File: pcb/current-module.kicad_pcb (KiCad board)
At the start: 4 copper layers, 50 x 50 mm, 128 parts, among them J2 SWD Header, SW1 SKRPABE010, U1 STM32C051G8Ux, U2 A1324LLHLT-T, U3 A1324LLHLT-T, U4 TLV9064, Y1 ECS-480-10-37B2-RWN-TR

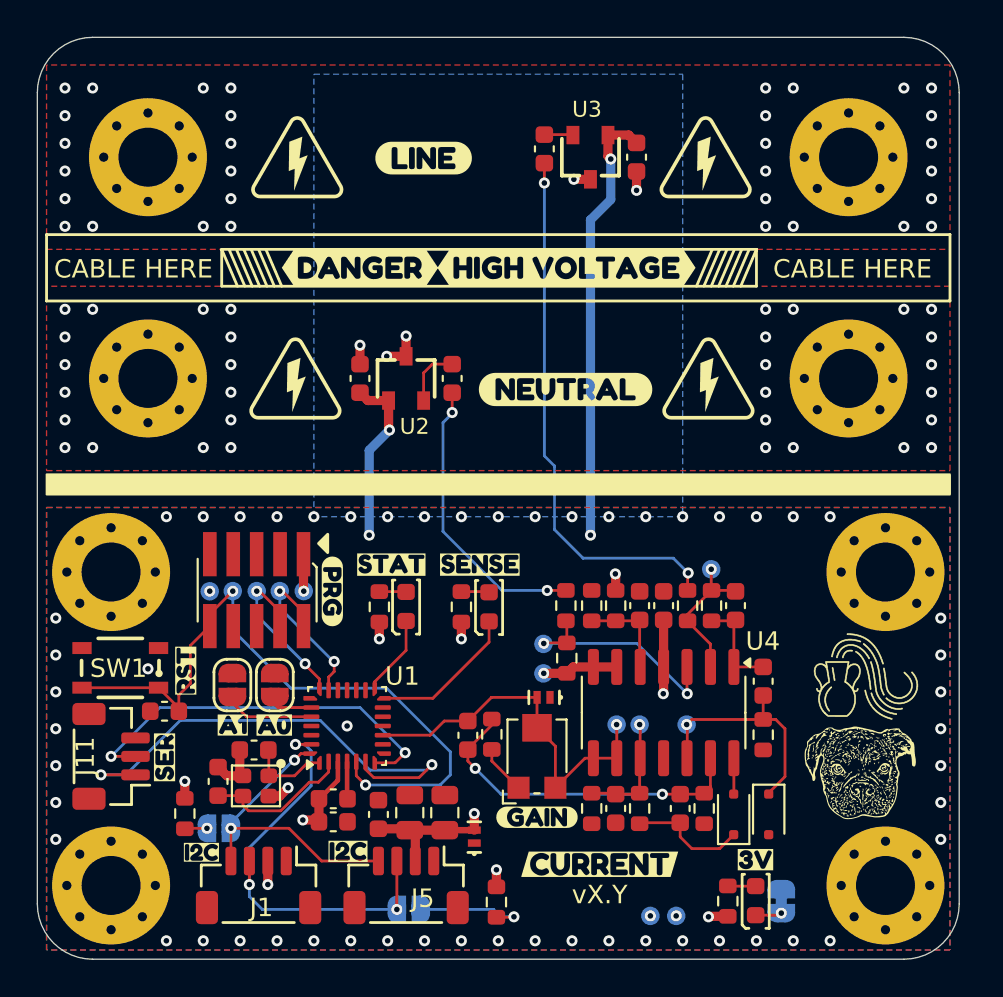
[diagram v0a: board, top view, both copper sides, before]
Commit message: Updated part silkscreen
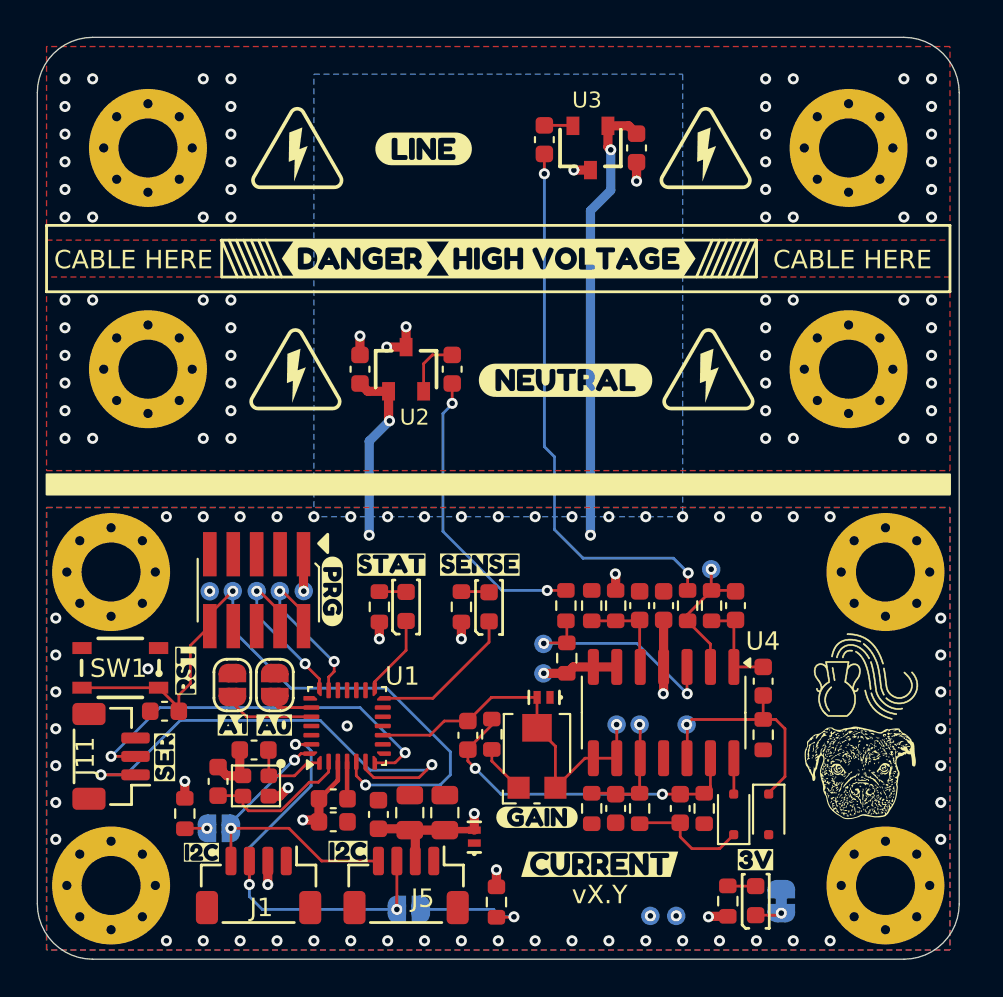
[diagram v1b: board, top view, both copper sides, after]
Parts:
- moved C11 0.50 mm to (67.5, 118.0)
- moved C7 0.50 mm to (77.5, 105.5)
- moved C8 0.50 mm to (72.5, 118.0)
- moved C9 0.50 mm to (82.5, 106.0)
- moved H5 0.50 mm to (56.0, 106.0)
- moved H6 0.50 mm to (94.0, 106.0)
- moved H7 0.50 mm to (56.0, 118.0)
- moved H8 0.50 mm to (94.0, 118.0)
- moved SYM1 0.50 mm to (86.2, 106.0)
- moved SYM2 0.50 mm to (64.1, 106.0)
- moved SYM5 0.50 mm to (64.0, 118.0)
- moved SYM6 0.50 mm to (86.4, 118.0)
- moved U2 0.50 mm to (70.0, 118.0)
- moved U3 0.50 mm to (80.0, 106.0)
- moved kibuzzard-68F7E620 0.50 mm to (67.5, 112.0)
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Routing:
- net +3.3V: track 59.1 -> 60.1 mm
- net /Current Sensor/H2IN: track 29.3 -> 29.8 mm
